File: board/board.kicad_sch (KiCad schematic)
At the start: 2 parts

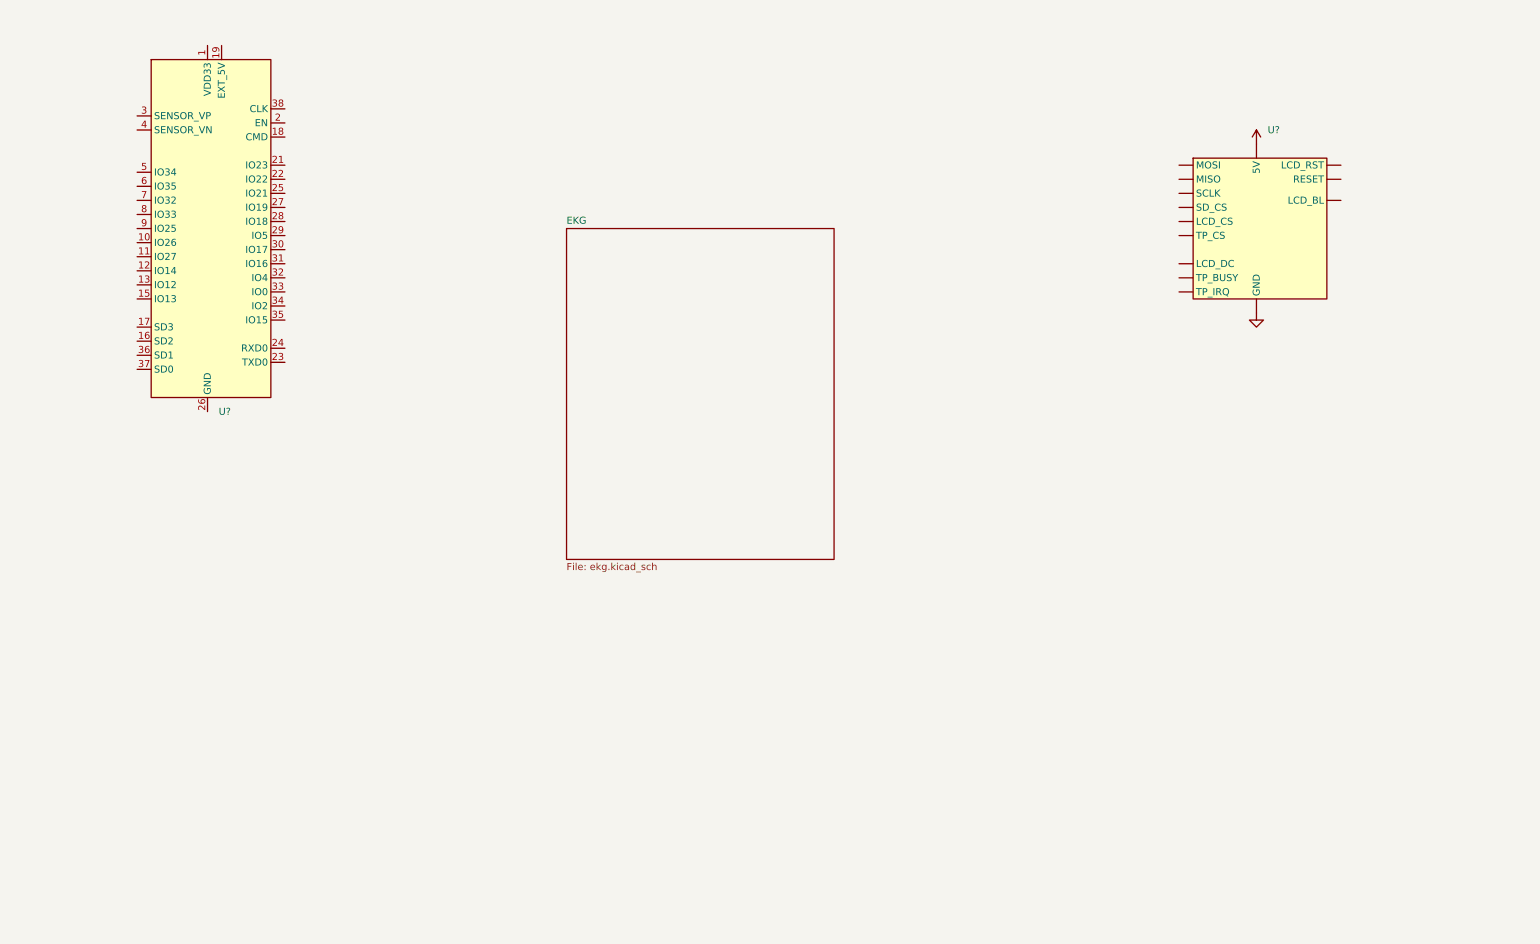
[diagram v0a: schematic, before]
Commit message: added ekg chip
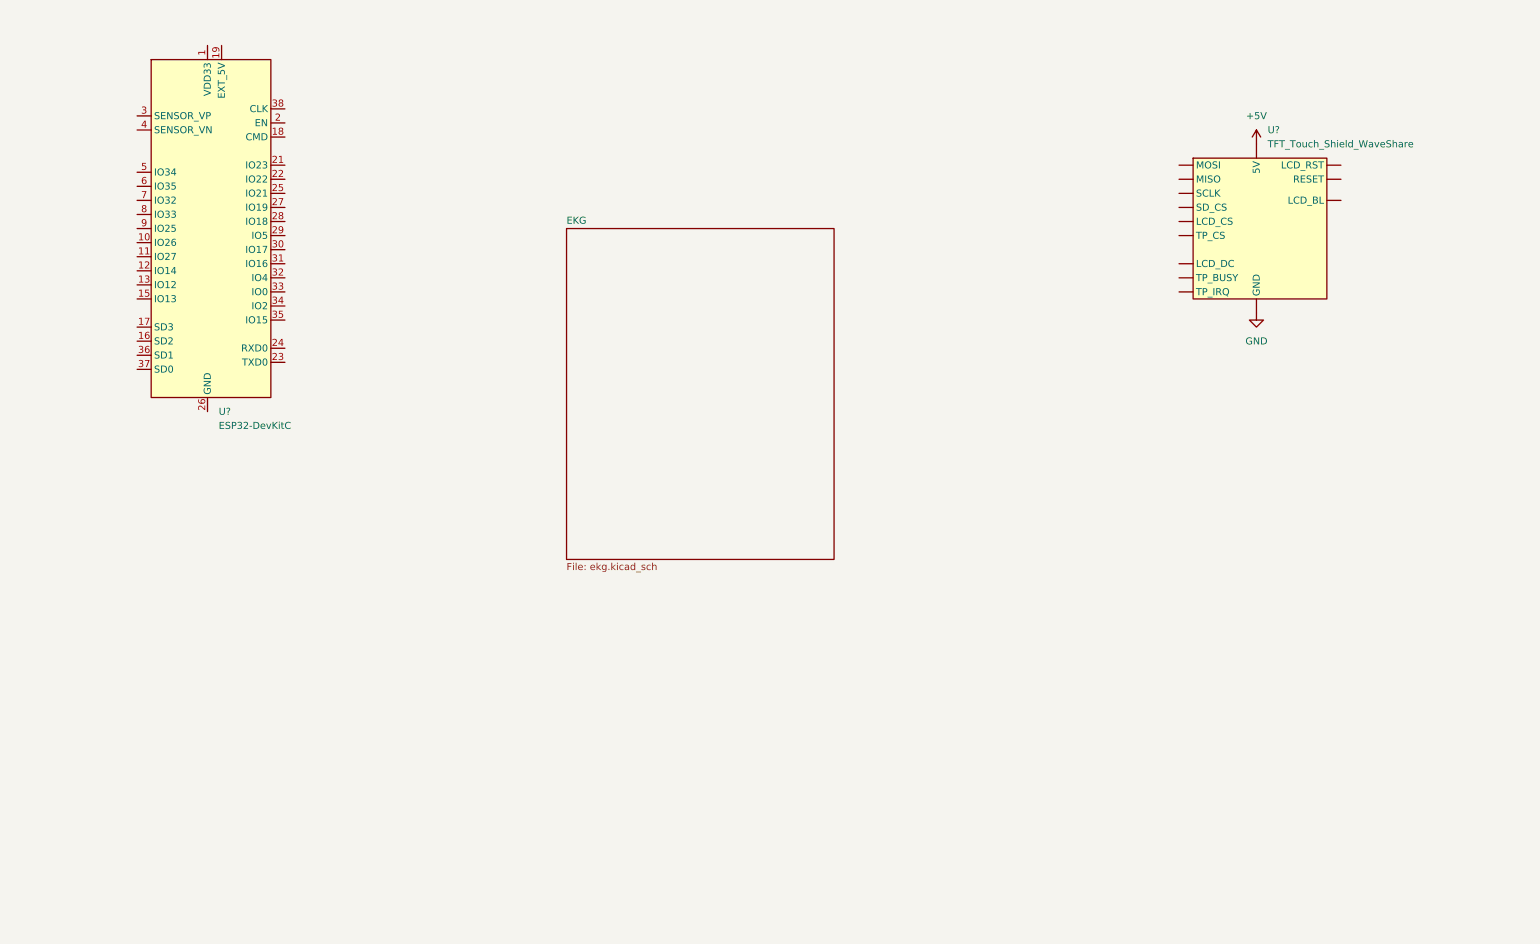
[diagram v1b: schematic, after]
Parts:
- U?: value (none) -> TFT_Touch_Shield_WaveShare
- U?: value (none) -> ESP32-DevKitC

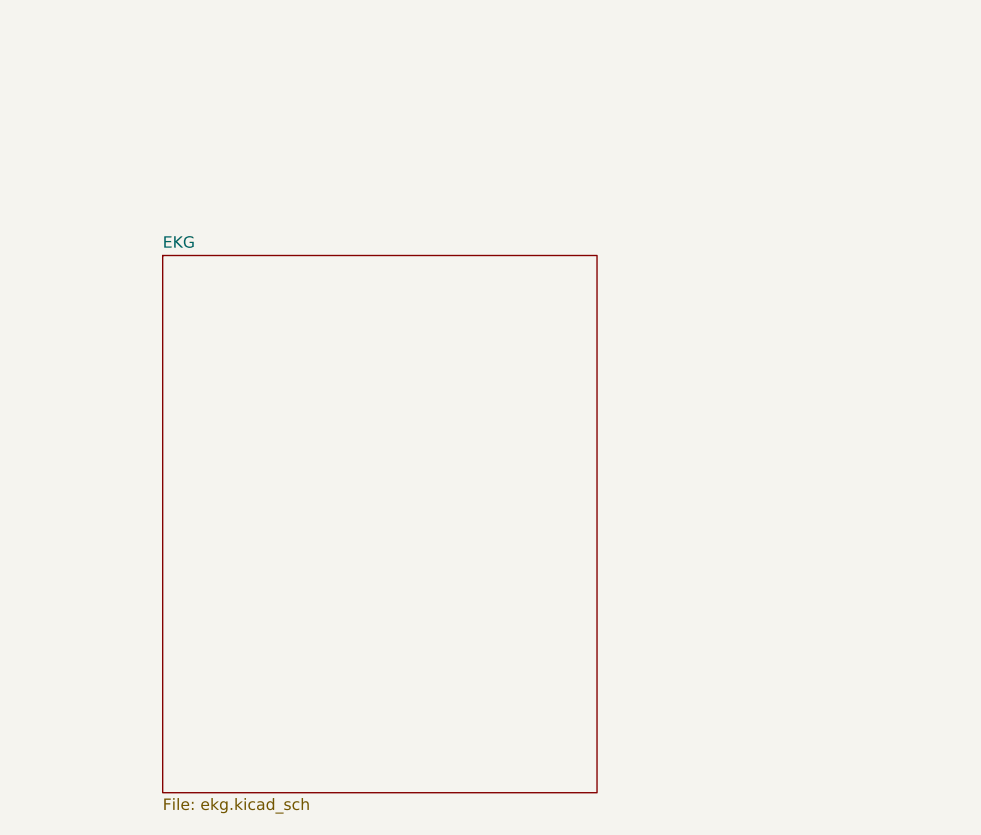
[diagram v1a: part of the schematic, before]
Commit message: added filter and imu
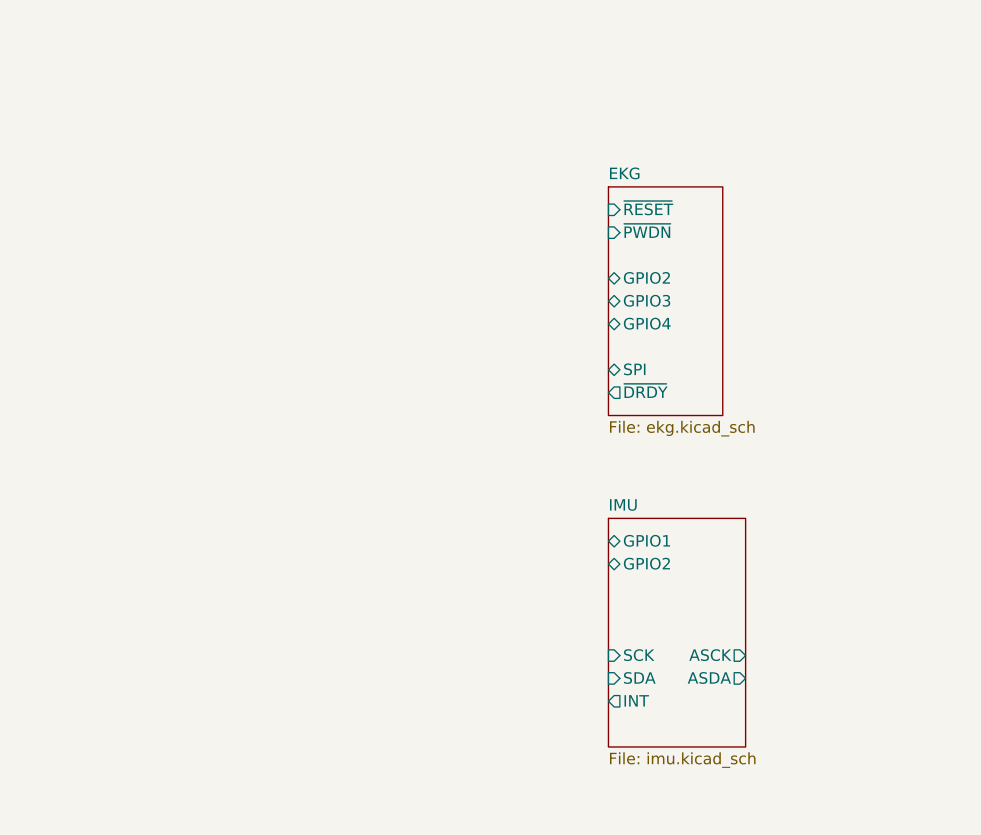
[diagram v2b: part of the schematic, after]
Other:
- added sheet IMU (imu.kicad_sch)
- sheet EKG ports: added GPIO2, GPIO3, GPIO4, SPI, ~{DRDY}, ~{PWDN}, ~{RESET}; removed none

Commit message: updated schematic
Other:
- added sheet ACD (adc.kicad_sch)
- added sheet PowerSupply (power_supply.kicad_sch)

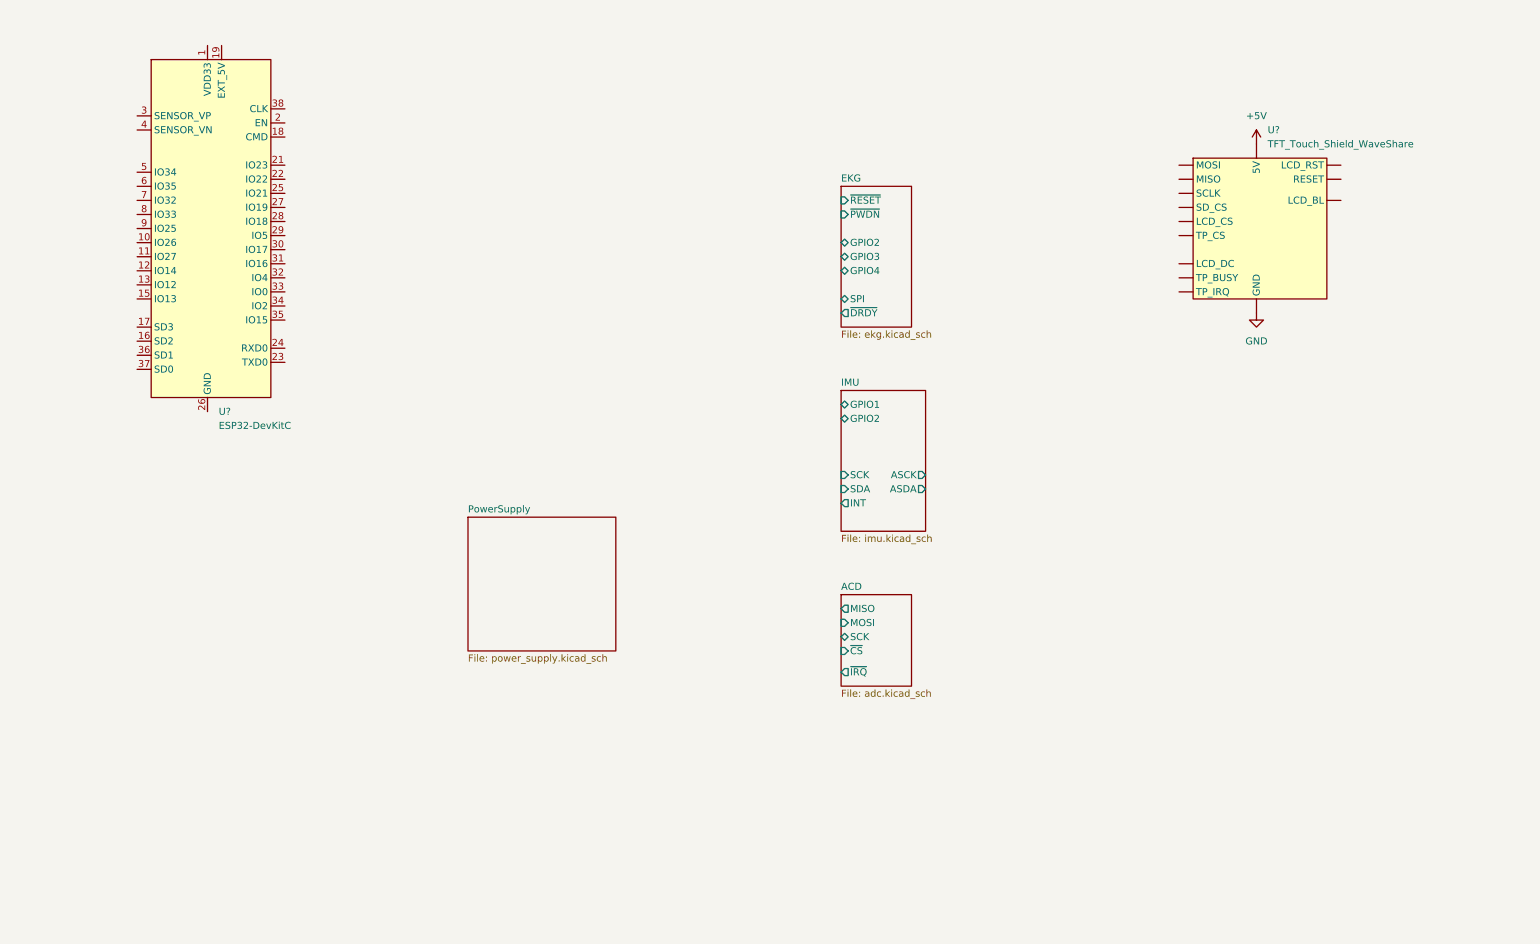
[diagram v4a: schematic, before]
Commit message: added SD card and pulsoxy
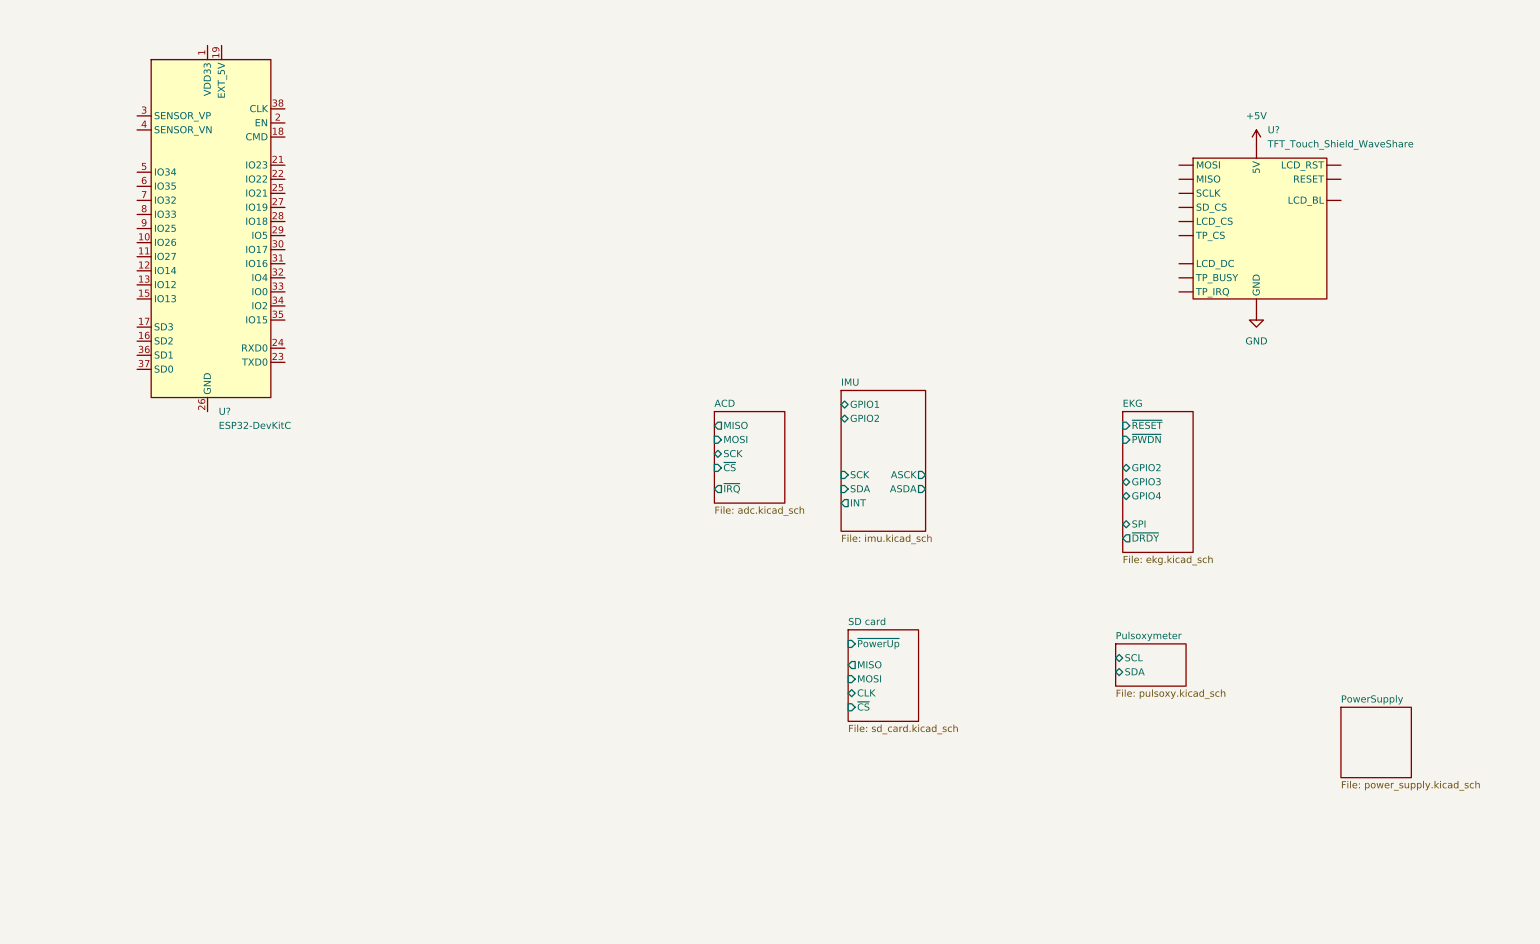
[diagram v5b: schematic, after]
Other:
- added sheet Pulsoxymeter (pulsoxy.kicad_sch)
- added sheet SD card (sd_card.kicad_sch)

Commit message: updated schematic after review
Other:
- sheet ACD renamed ADC
- sheet EKG ports: added GPIO1; removed none
- note added: "TODO: SD-Karte Pulsoxy"
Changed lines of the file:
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@@
 (kicad_sch (version 20211123) (generator eeschema)
   (paper "A4")
+  (text "TODO:\nSD-Karte\nPulsoxy" (at 109.22 62.23 0)
+    (effects (font (size 1.27 1.27)) (justify left bottom))
+  )
   (symbol (lib_id "ownLib:TFT_Touch_Shield_WaveShare") (at 238.76 59.69 0) (unit 1)
     (in_bom yes) (on_board yes) (fields_autoplaced)
@@
     )
   )
-  (sheet (at 140.97 93.98) (size 12.7 16.51) (fields_autoplaced)
-    (stroke (width 0.1524) (type solid) (color 0 0 0 0))
-    (fill (color 0 0 0 0.0000))
-    (property "Sheet name" "ACD" (id 0) (at 140.97 93.2684 0)
-      (effects (font (size 1.27 1.27)) (justify left bottom))
-    )
-    (property "Sheet file" "adc.kicad_sch" (id 1) (at 140.97 111.0746 0)
-      (effects (font (size 1.27 1.27)) (justify left top))
-    )
-    (pin "MOSI" input (at 140.97 99.06 180)
-      (effects (font (size 1.27 1.27)) (justify left))
-    )
-    (pin "MISO" output (at 140.97 96.52 180)
-      (effects (font (size 1.27 1.27)) (justify left))
-    )
-    (pin "SCK" bidirectional (at 140.97 101.6 180)
-      (effects (font (size 1.27 1.27)) (justify left))
-    )
-    (pin "~{CS}" input (at 140.97 104.14 180)
-      (effects (font (size 1.27 1.27)) (justify left))
-    )
-    (pin "~{IRQ}" output (at 140.97 107.95 180)
+  (sheet (at 140.97 104.14) (size 12.7 16.51)
+    (stroke (width 0.1524) (type solid) (color 0 0 0 0))
+    (fill (color 0 0 0 0.0000))
+    (property "Sheet name" "ADC" (id 0) (at 140.97 104.14 0)
+      (effects (font (size 1.27 1.27)) (justify left bottom))
+    )
+    (property "Sheet file" "adc.kicad_sch" (id 1) (at 140.97 121.2346 0)
+      (effects (font (size 1.27 1.27)) (justify left top))
+    )
+    (pin "MOSI" input (at 140.97 109.22 180)
+      (effects (font (size 1.27 1.27)) (justify left))
+    )
+    (pin "MISO" output (at 140.97 106.68 180)
+      (effects (font (size 1.27 1.27)) (justify left))
+    )
+    (pin "SCK" bidirectional (at 140.97 111.76 180)
+      (effects (font (size 1.27 1.27)) (justify left))
+    )
+    (pin "~{CS}" input (at 140.97 114.3 180)
+      (effects (font (size 1.27 1.27)) (justify left))
+    )
+    (pin "~{IRQ}" output (at 140.97 118.11 180)
       (effects (font (size 1.27 1.27)) (justify left))
     )
@@
       (effects (font (size 1.27 1.27)) (justify left))
     )
-    (pin "GPIO4" bidirectional (at 214.63 109.22 180)
-      (effects (font (size 1.27 1.27)) (justify left))
-    )
-    (pin "GPIO3" bidirectional (at 214.63 106.68 180)
-      (effects (font (size 1.27 1.27)) (justify left))
-    )
-    (pin "GPIO2" bidirectional (at 214.63 104.14 180)
+    (pin "GPIO4" bidirectional (at 214.63 93.98 180)
+      (effects (font (size 1.27 1.27)) (justify left))
+    )
+    (pin "GPIO3" bidirectional (at 214.63 93.98 180)
+      (effects (font (size 1.27 1.27)) (justify left))
+    )
+    (pin "GPIO2" bidirectional (at 214.63 93.98 180)
       (effects (font (size 1.27 1.27)) (justify left))
     )
@@
     )
     (pin "~{PWDN}" input (at 214.63 99.06 180)
+      (effects (font (size 1.27 1.27)) (justify left))
+    )
+    (pin "GPIO1" bidirectional (at 214.63 93.98 180)
       (effects (font (size 1.27 1.27)) (justify left))
     )
@@
       (reference "#PWR?") (unit 1) (value "+3.3VA") (footprint "")
     )
+    (path "/db6b8362-1493-4107-af7d-a8faca8bb053/5b87a2ce-4929-417b-95fa-cd030e59a5ec"
+      (reference "#PWR?") (unit 1) (value "+3V3") (footprint "")
+    )
     (path "/0133fba6-5aa6-4171-8a60-95549c0db33b/5ba70fc5-860b-413d-b200-2c0dbf8bb502"

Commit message: updated schematic
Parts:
- added R? (x2): 10k, symbol Device:R_Small
- added TP?: ASCK, symbol Connector:TestPoint
- added TP? (x2): G1, symbol Connector:TestPoint
- added TP? (x2): G4, symbol Connector:TestPoint
- added TP?: G2, symbol Connector:TestPoint
- added TP?: ASDA, symbol Connector:TestPoint
- added TP?: MOSI, symbol Connector:TestPoint
- added TP?: PUP, symbol Connector:TestPoint
- added TP? (x2): CS, symbol Connector:TestPoint
- added TP?: MISO, symbol Connector:TestPoint
- added TP?: POK, symbol Connector:TestPoint
- added TP? (x2): SCK, symbol Connector:TestPoint
- added TP?: SDA, symbol Connector:TestPoint
- added TP?: G3, symbol Connector:TestPoint
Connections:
- net EKG/GPIO1: now also TP?.1
- net IMU/ASCK: now also TP?.1
- net IMU/ASDA: now also TP?.1
- net IMU/GPIO1: now also TP?.1
- net IMU/GPIO2: now also TP?.1
- net TOUCH_Y-: now reaches U?. (SCLK)
- net TOUCH_Y-: now also U?.33 (IO0)
- net +3V3: now reaches U?.1 (VDD33)
- net +3V3: now also R?.1, R?.1
- net TOUCH_X-: now reaches U?.11 (IO27)
- net TOUCH_X-: now also U?. (SCLK)
- net HSPI_SCK: now reaches U?.12 (IO14)
- net HSPI_SCK: now also U?. (SCLK)
- net HSPI_MISO: now reaches U?.13 (IO12)
- net HSPI_MISO: now also U?. (SCLK)
- net HSPI_MOSI: now reaches U?.15 (IO13)
- net HSPI_MOSI: now also U?. (SCLK)
- net VSPI_MOSI: now reaches U?.21 (IO23)
- net VSPI_MOSI: now also TP?.1
- net I2C1_SCK: now reaches U?.22 (IO22)
- net I2C1_SCK: now also R?.2, TP?.1
- net I2C1_SDA: now reaches U?.25 (IO21)
- net I2C1_SDA: now also R?.2, TP?.1
- net VSPI_MISO: now reaches U?.27 (IO19)
- net VSPI_MISO: now also TP?.1
- net VSPI_SCK: now reaches U?.28 (IO18)
- net VSPI_SCK: now also TP?.1
- net EKG_CS: now reaches U?.29 (IO5)
- net EKG_CS: now also TP?.1
- net ~{EKG_INT}: now reaches U?.3 (SENSOR_VP)
- net ADC_CS: now reaches U?.30 (IO17)
- net ADC_CS: now also TP?.1
- net SD_CS: now reaches U?.31 (IO16)
- net TOUCH_Y+: now reaches U?.32 (IO4)
- net TOUCH_Y+: now also U?. (SCLK)
- net TOUCH_X+: now reaches U?.34 (IO2)
- net TOUCH_X+: now also U?. (SCLK)
- net HSPI_CS: now reaches U?.35 (IO15)
- net HSPI_CS: now also U?. (SCLK)
- net IMU_INT: now reaches U?.4 (SENSOR_VN)
- net ~{ADC_INT}: now reaches U?.5 (IO34)
- net ~{SDPowerOK}: now reaches U?.6 (IO35)
- net ~{SDPowerOK}: now also TP?.1
- net ~{SDPowerUp}: now reaches U?.7 (IO32)
- net ~{SDPowerUp}: now also TP?.1
- net ~{EKGReset}: now reaches U?.8 (IO33)
- net ~{EKGPowerDown}: now reaches U?.9 (IO25)
- new net EKG/GPIO2: TP?.1
- new net EKG/GPIO3: TP?.1
- new net EKG/GPIO4: TP?.1
- new net LCD_BL: U?. (SCLK)
- new net LCD_DC: U?. (SCLK)
- new net LCD_RST: U?. (SCLK)
- no-connect marks 0 -> 12
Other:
- sheet EKG ports: added CLK, MISO, MOSI, ~{CS}; removed SPI
- sheet SD card ports: added ~{PowerOK}; removed none
- note added: "TODO: I2C devices with MOSFET on switched pwrsupply"
- note removed: "TODO: SD-Karte Pulsoxy"
- moved on the sheet: U?
